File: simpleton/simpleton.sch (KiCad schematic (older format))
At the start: 0 parts

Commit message: Created STM32F405RG component
Closes #1
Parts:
- added U?: STM32F405RG, symbol STM32F405RG
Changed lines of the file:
@@
 LIBS:contrib
 LIBS:valves
+LIBS:simpleton-cache
 EELAYER 25 0
 EELAYER END
@@
 Comment4 ""
 $EndDescr
+$Comp
+L STM32F405RG U?
+U 1 1 56D00203
+P 2350 900
+F 0 "U?" H 2350 -2700 60  0000 C CNN
+F 1 "STM32F405RG" H 2350 800 60  0000 C CNN
+F 2 "" H 2350 900 60  0000 C CNN
+F 3 "" H 2350 900 60  0000 C CNN
+	1    2350 900
+	1    0    0    -1
+$EndComp
 $EndSCHEMATC

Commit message: Added MCU power supply circuitry
Closes #2
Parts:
- added C?: 22nF, symbol C_Small
- added C? (x3): 10uF, symbol C_Small
- added C?: 150pF, symbol C_Small
- added C? (x6): 100nF, symbol C_Small
- added C?: 22uF, symbol C_Small
- added C?: 1uF, symbol C_Small
- added C? (x2): 2.2uF, symbol C_Small
- added C?: 4.7uF, symbol C_Small
- added D? (x3): D_Schottky_Small, symbol D_Schottky_Small
- added J?: USB_MICROB, symbol USB_MICROB
- added L?: 15uH, symbol INDUCTOR_SMALL
- added P?: CONN_01X02, symbol CONN_01X02
- added R? (x2): 100k, symbol R_Small
- added R?: 40.2k, symbol R_Small
- added R?: 210k, symbol R_Small
- added U?: RT9193-GB, symbol RT9193-GB
- added U?: MP1584, symbol MP1584
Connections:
- net labels added: GND, REG_5V, VBUS, VCAP1, VCAP2, VCC_3_3V, VCC_5V, VCC_LIPO, VDD1, VDD2, VDD3, VDD4, VDDA
- wire segments 0 -> 78

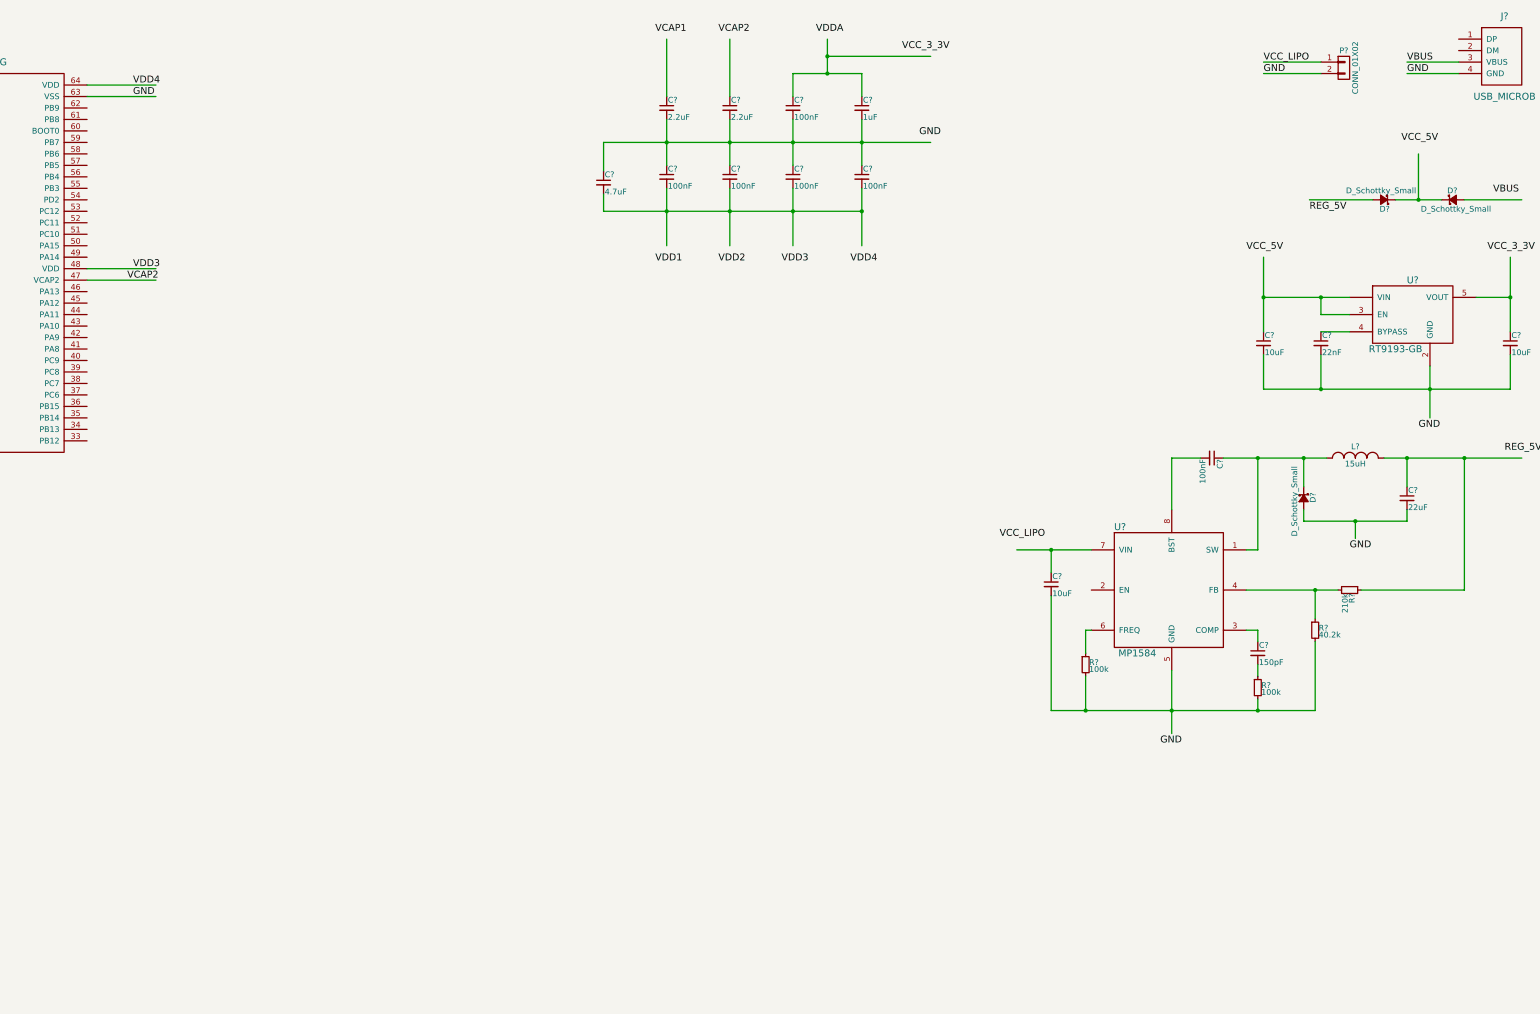
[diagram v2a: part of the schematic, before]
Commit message: Added CP2104
Closes #3

- Created CP2104 part
- Added CP2104 to schematic and wired to USB power and USART1
- Added datasheet
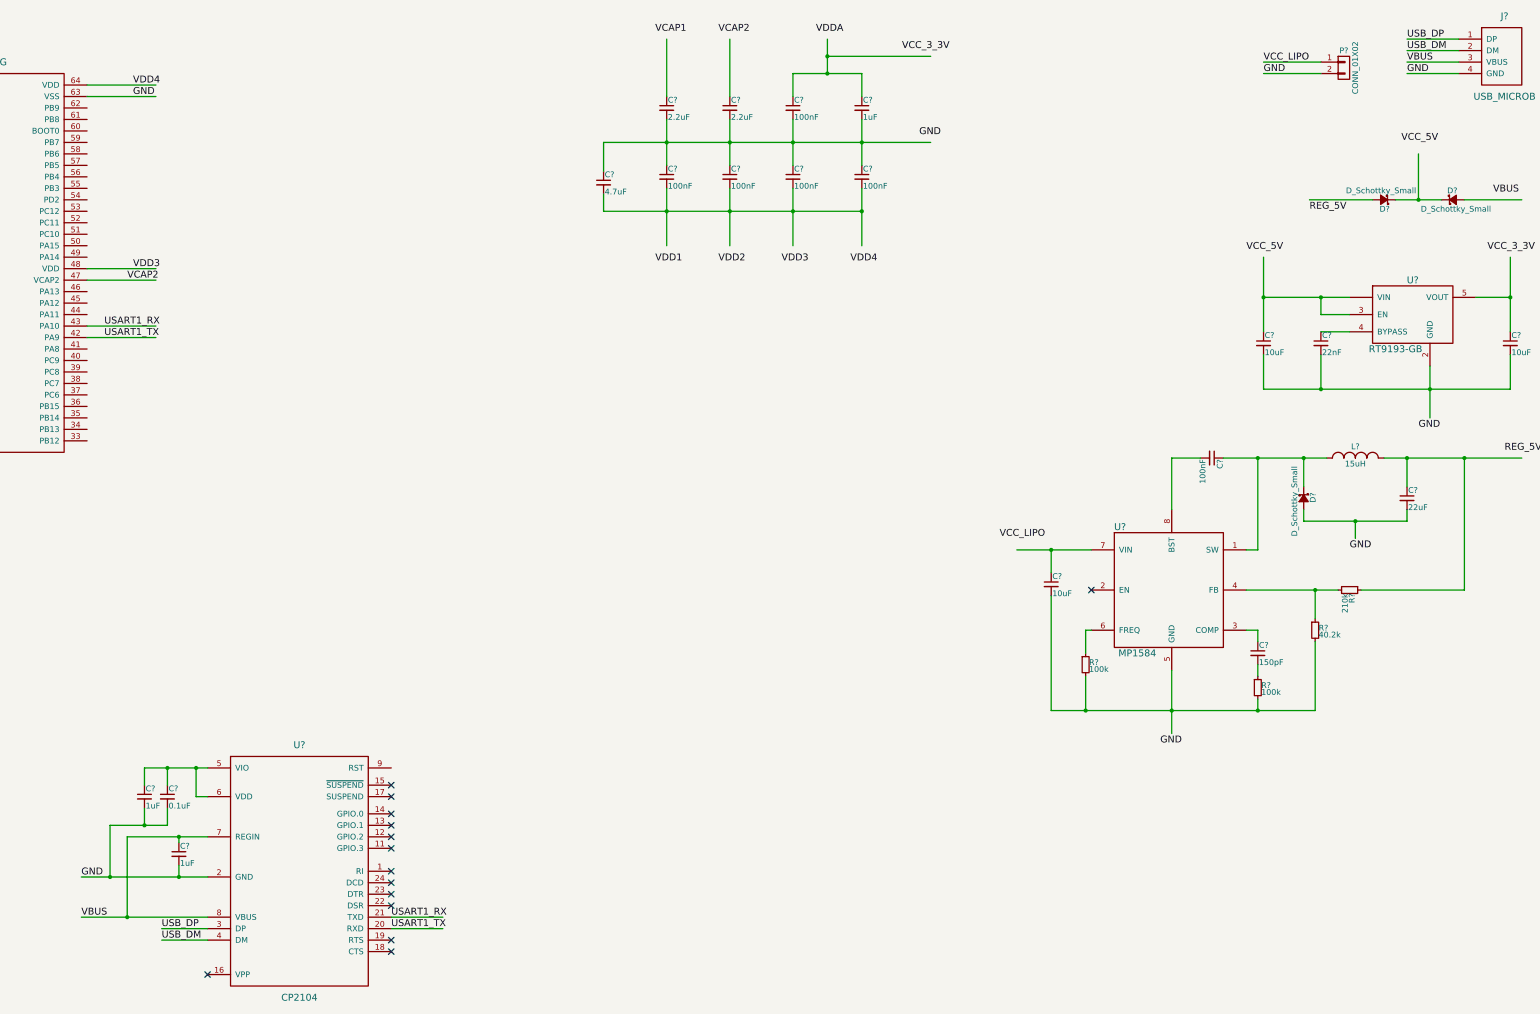
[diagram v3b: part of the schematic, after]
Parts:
- added C?: 0.1uF, symbol C_Small
- added C? (x2): 1uF, symbol C_Small
- added U?: CP2104, symbol CP2104
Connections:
- net labels added: USART1_RX, USART1_TX, USB_DM, USB_DP
- wire segments 78 -> 101
- no-connect marks 0 -> 14
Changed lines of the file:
@@
 Text Label 10000 2750 0    60   ~ 0
 VDD4
+Text Label 10450 900  0    60   ~ 0
+VCC_3_3V
+$Comp
+L CP2104 U?
+U 1 1 56D2AFA7
+P 5200 6850
+F 0 "U?" H 5200 6750 60  0000 C CNN
+F 1 "CP2104" H 5200 4550 60  0000 C CNN
+F 2 "" H 5200 6850 60  0000 C CNN
+F 3 "" H 5200 6850 60  0000 C CNN
+	1    5200 6850
+	1    0    0    -1
+$EndComp
+Text Label 14850 900  0    60   ~ 0
+USB_DM
+Text Label 14850 800  0    60   ~ 0
+USB_DP
+NoConn ~ 12100 5600
+NoConn ~ 6000 7300
+NoConn ~ 6000 7400
+NoConn ~ 6000 7550
+NoConn ~ 6000 7650
+NoConn ~ 6000 7750
+NoConn ~ 6000 7850
+NoConn ~ 6000 8050
+NoConn ~ 6000 8150
+NoConn ~ 6000 8250
+NoConn ~ 6000 8350
+NoConn ~ 6000 8650
+NoConn ~ 6000 8750
+NoConn ~ 4400 8950
+Text Label 4000 8550 0    60   ~ 0
+USB_DP
+Text Label 4000 8650 0    60   ~ 0
+USB_DM
+Text Label 3300 8450 0    60   ~ 0
+VBUS
+$Comp
+L C_Small C?
+U 1 1 56D2DE4A
+P 4050 7400
+F 0 "C?" H 4060 7470 50  0000 L CNN
+F 1 "0.1uF" H 4060 7320 50  0000 L CNN
+F 2 "" H 4050 7400 60  0000 C CNN
+F 3 "" H 4050 7400 60  0000 C CNN
+	1    4050 7400
+	1    0    0    -1
+$EndComp
+$Comp
+L C_Small C?
+U 1 1 56D2DEC8
+P 3850 7400
+F 0 "C?" H 3860 7470 50  0000 L CNN
+F 1 "1uF" H 3860 7320 50  0000 L CNN
+F 2 "" H 3850 7400 60  0000 C CNN
+F 3 "" H 3850 7400 60  0000 C CNN
+	1    3850 7400
+	1    0    0    -1
+$EndComp
+Text Label 3300 8100 0    60   ~ 0
+GND
+$Comp
+L C_Small C?
+U 1 1 56D2E6A5
+P 4150 7900
+F 0 "C?" H 4160 7970 50  0000 L CNN
+F 1 "1uF" H 4160 7820 50  0000 L CNN
+F 2 "" H 4150 7900 60  0000 C CNN
+F 3 "" H 4150 7900 60  0000 C CNN
+	1    4150 7900
+	1    0    0    -1
+$EndComp
 Connection ~ 13600 3050
 Connection ~ 14100 3050
@@
 	9800 950  10700 950
 Connection ~ 9800 950
-Text Label 10450 900  0    60   ~ 0
-VCC_3_3V
+Wire Wire Line
+	15300 800  14850 800
+Wire Wire Line
+	15300 900  14850 900
+Wire Wire Line
+	4400 8550 4000 8550
+Wire Wire Line
+	4400 8650 4000 8650
+Wire Wire Line
+	3300 8100 4400 8100
+Wire Wire Line
+	4400 8450 3300 8450
+Wire Wire Line
+	3700 8450 3700 7750
+Wire Wire Line
+	3700 7750 4400 7750
+Connection ~ 3700 8450
+Wire Wire Line
+	4400 7400 4300 7400
+Wire Wire Line
+	4300 7400 4300 7150
+Connection ~ 4300 7150
+Wire Wire Line
+	3850 7150 4400 7150
+Wire Wire Line
+	4050 7150 4050 7300
+Wire Wire Line
+	3850 7150 3850 7300
+Connection ~ 4050 7150
+Wire Wire Line
+	4050 7500 4050 7650
+Wire Wire Line
+	4050 7650 3550 7650
+Wire Wire Line
+	3550 7650 3550 8100
+Connection ~ 3550 8100
+Wire Wire Line
+	3850 7500 3850 7650
+Connection ~ 3850 7650
+Wire Wire Line
+	4150 7750 4150 7800
+Connection ~ 4150 7750
+Wire Wire Line
+	4150 8000 4150 8100
+Connection ~ 4150 8100
+Wire Wire Line
+	6000 8450 6450 8450
+Wire Wire Line
+	6000 8550 6450 8550
+Wire Wire Line
+	3350 3400 3950 3400
+Wire Wire Line
+	3350 3300 3950 3300
+Text Label 3500 3400 0    60   ~ 0
+USART1_TX
+Text Label 3500 3300 0    60   ~ 0
+USART1_RX
+Text Label 6000 8550 0    60   ~ 0
+USART1_TX
+Text Label 6000 8450 0    60   ~ 0
+USART1_RX
 $EndSCHEMATC

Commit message: Added MPU6000
Closes #5

- Added MPU6000 data sheet
- Created MPU6000 component
- Connected MPU6000 to power and SPI_1
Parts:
- added C? (x2): 0.1uF, symbol C_Small
- added C?: 2.2nF, symbol C_Small
- added U?: MPU6000, symbol MPU6000
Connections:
- net labels added: SPI_1_CS, SPI_1_MISO, SPI_1_MOSI, SPI_1_SCLK
- wire segments 101 -> 122
- no-connect marks 14 -> 28
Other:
- moved on the sheet: C?, D?, L?, R?, U?

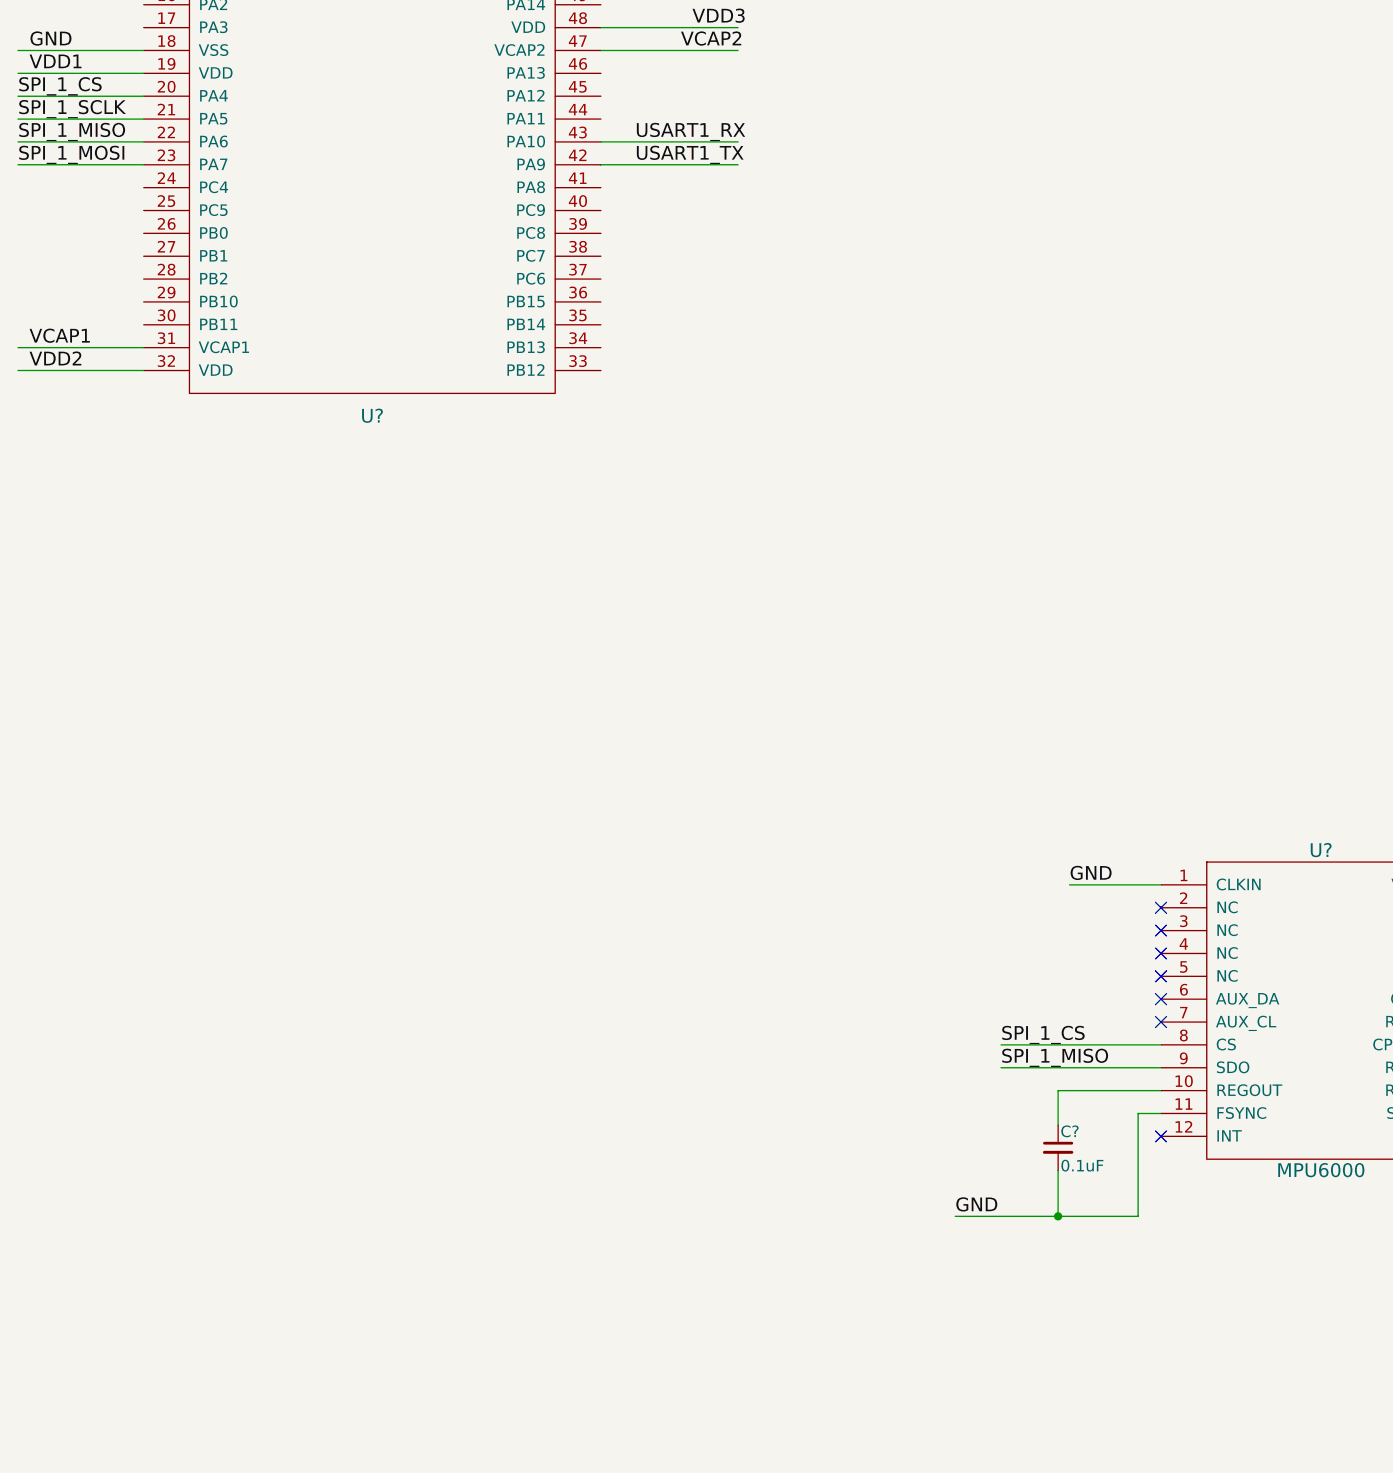
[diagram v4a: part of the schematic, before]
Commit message: Connected MPU interrupt pin to MCU
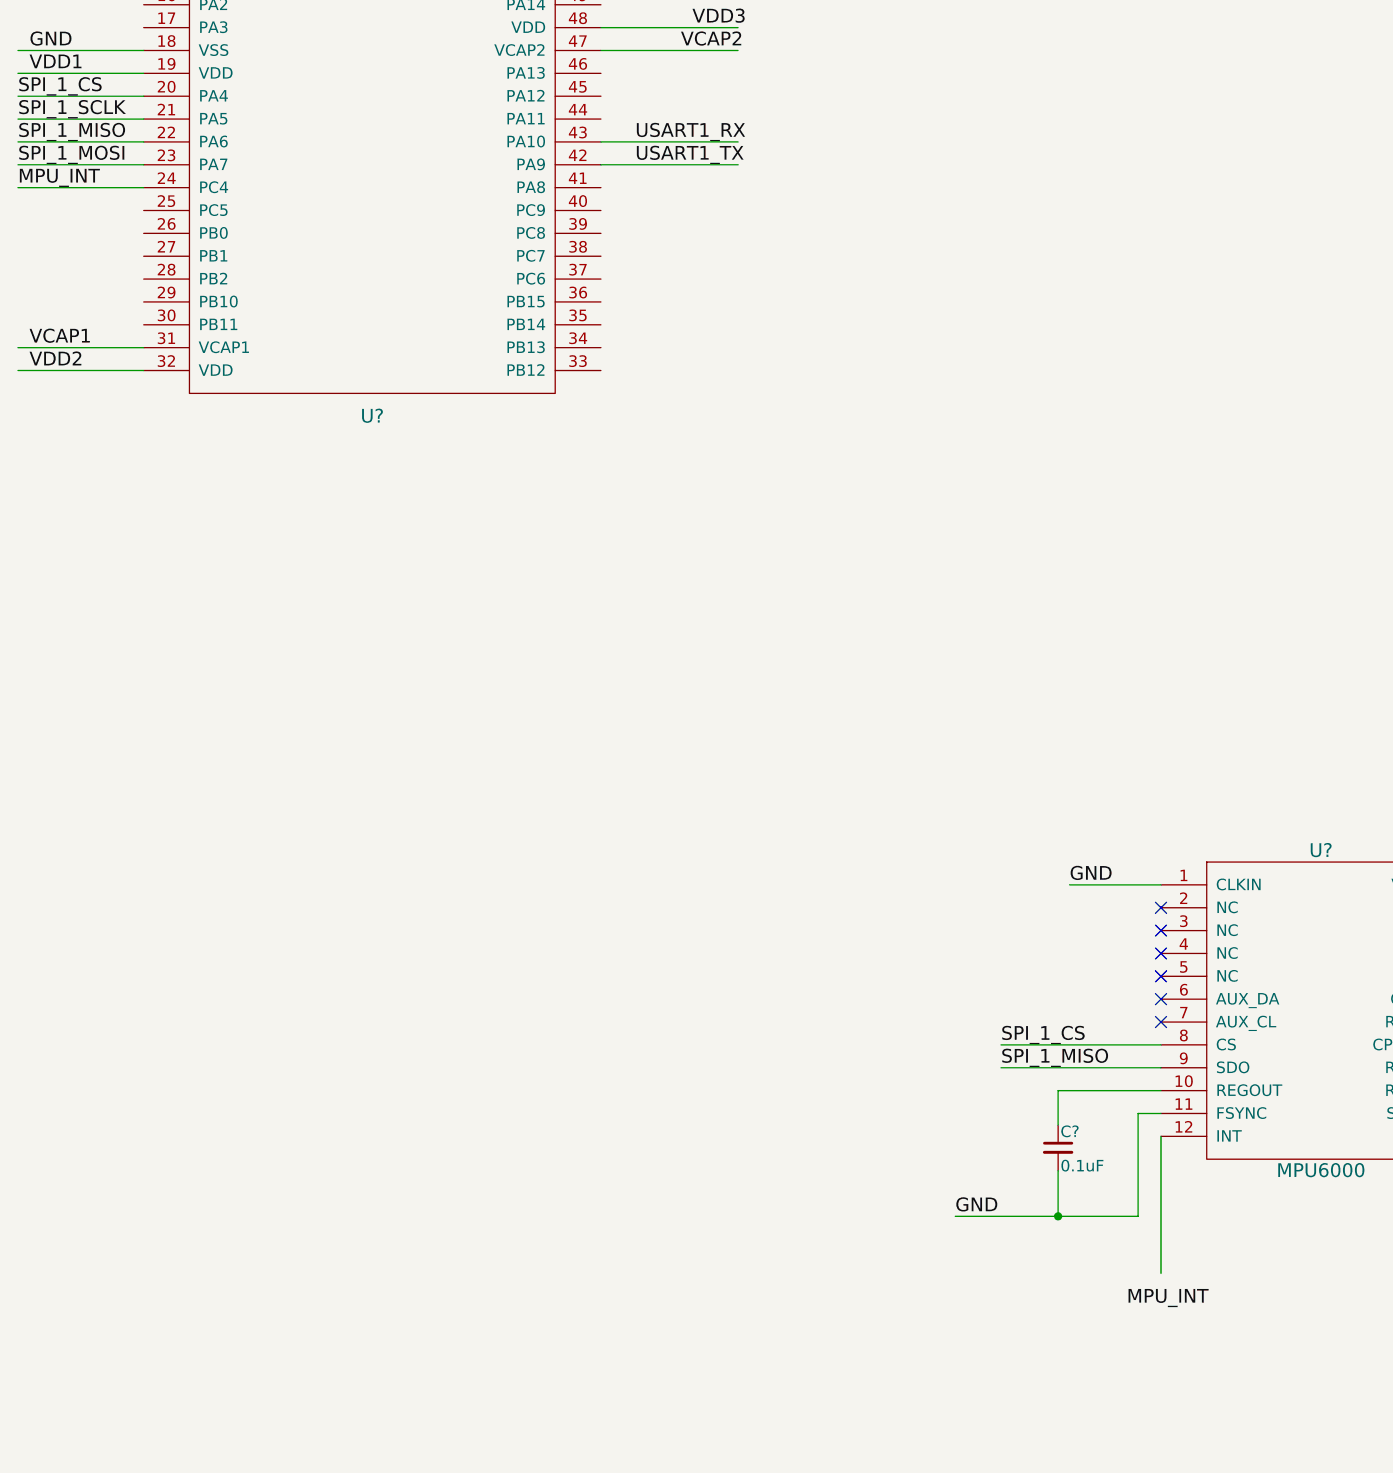
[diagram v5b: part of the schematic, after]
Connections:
- net labels added: MPU_INT
- wire segments 122 -> 124
- no-connect marks 28 -> 27
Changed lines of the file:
@@
 Text Label 5100 7350 0    60   ~ 0
 SPI_1_MISO
-NoConn ~ 5800 7650
 NoConn ~ 7200 6650
 NoConn ~ 7200 6750
@@
 Text Label 800  3400 0    60   ~ 0
 SPI_1_MOSI
+Wire Wire Line
+	5800 7650 5800 8250
+Text Label 5650 8400 0    60   ~ 0
+MPU_INT
+Wire Wire Line
+	1350 3500 800  3500
+Text Label 800  3500 0    60   ~ 0
+MPU_INT
 $EndSCHEMATC
